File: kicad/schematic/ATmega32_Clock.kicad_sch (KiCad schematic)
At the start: 0 parts

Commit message: Restored full KiCad schematic and PCB layouts from original AI generation prior to truncation
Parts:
- added C1, C2: 22pF, Capacitor_THT:C_Disc_D3.0mm_W1.6mm_P2.50mm, symbol Device:C
- added C3, C4: 100nF, Capacitor_THT:C_Disc_D3.0mm_W1.6mm_P2.50mm, symbol Device:C
- added D1: STATUS, LED_THT:LED_D3.0mm, symbol Device:LED
- added D2: TASK, LED_THT:LED_D3.0mm, symbol Device:LED
- added J1: USART, Connector_PinHeader_2.54mm:PinHeader_1x02_P2.54mm_Vertical, symbol Connector_Generic:Conn_01x02
- added J2: ISP, Connector_PinHeader_2.54mm:PinHeader_2x03_P2.54mm_Vertical, symbol Connector_Generic:Conn_02x03_Odd_Even
- added R1, R2, R3, R4: 10K, Resistor_THT:R_Axial_DIN0207_L6.3mm_D2.5mm_P10.16mm_Horizontal, symbol Device:R
- added R5, R6: 330R, Resistor_THT:R_Axial_DIN0207_L6.3mm_D2.5mm_P10.16mm_Horizontal, symbol Device:R
- added SW1: RESET, Button_Switch_THT:SW_PUSH_6mm, symbol Switch:SW_Push
- added SW2: SET, Button_Switch_THT:SW_PUSH_6mm, symbol Switch:SW_Push
- added SW3: INCREMENT, Button_Switch_THT:SW_PUSH_6mm, symbol Switch:SW_Push
- added SW4: CLK_RST, Button_Switch_THT:SW_PUSH_6mm, symbol Switch:SW_Push
- added U1: ATmega32A-P, Package_DIP:DIP-40_W15.24mm, symbol MCU_Microchip_ATmega:ATmega32A-P
- added Y1: 8MHz, Crystal:Crystal_HC49-4H_Vertical, symbol Device:Crystal
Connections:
- new net: R1.2, SW1.2
- new net: R2.2, SW2.2
- new net: R3.2, SW3.2
- new net: R4.2, SW4.2
- new net: D1.1 (K), R5.2
- new net: D2.1 (K), R6.2
- new net GND: C1.2, C2.2, D1.2 (A), D2.2 (A), SW1.1, SW2.1, SW3.1, SW4.1
- new net VCC: R1.1, R2.1, R3.1, R4.1
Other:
- note added: "BUTTONS: SET(PA0) INC(PA1) RST(PA2) Active-low, 10K pull-ups"
- note added: "CLOCK: 8MHz Crystal 22pF load caps"
- note added: "LEDs: STATUS(PB0) TASK(PB1) 330R current limiters"
- note added: "TIMER1 CTC: OCR1A = 8000000/(1024*1) - 1 = 7812 Interrupt Rate: 1 Hz (1 second) Prescaler: 1024 | F_CPU: 8 MHz"

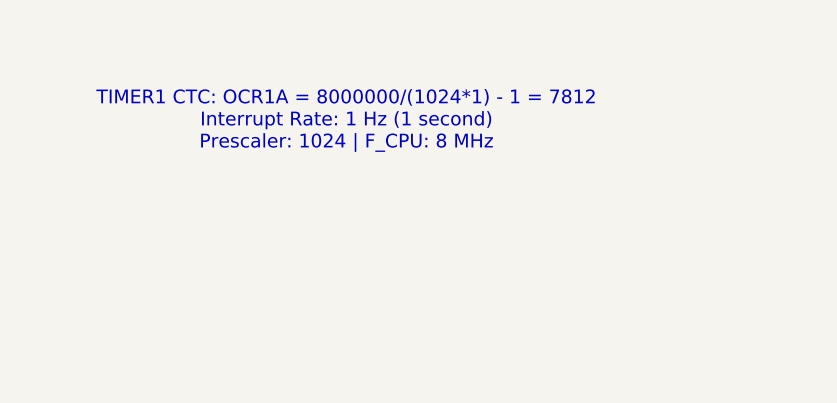
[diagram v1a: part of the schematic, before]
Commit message: Updated all documentation to reflect 10ms (100Hz) timer configuration
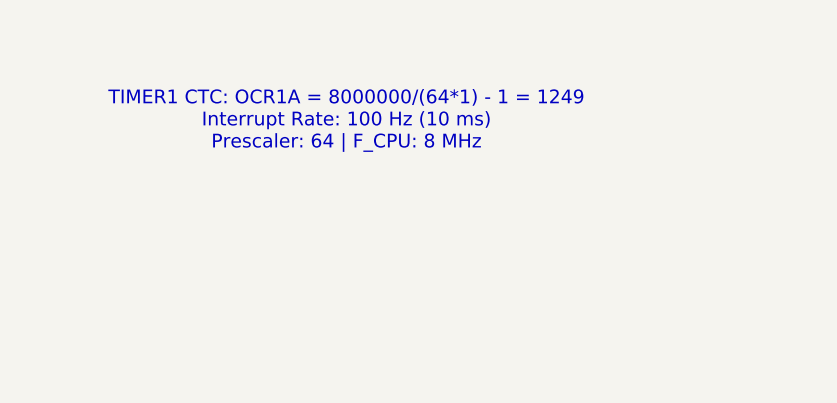
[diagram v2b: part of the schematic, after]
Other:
- note added: "TIMER1 CTC: OCR1A = 8000000/(64*1) - 1 = 1249 Interrupt Rate: 100 Hz (10 ms) Prescaler: 64 | F_CPU: 8 MHz"
- note removed: "TIMER1 CTC: OCR1A = 8000000/(1024*1) - 1 = 7812 Interrupt Rate: 1 Hz (1 second) Prescaler: 1024 | F_CPU: 8 MHz"
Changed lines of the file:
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@@
     (rev "1.0")
     (company "CT_321 PBL Project 08")
-    (comment 1 "Timer1 CTC | 8MHz Crystal | Prescaler 1024 | OCR1A=7812 | 1Hz Interrupt")
+    (comment 1 "Timer1 CTC | 8MHz Crystal | Prescaler 64 | OCR1A=1249 | 100Hz Interrupt")
     (comment 2 "Status LED: PB0 toggles 2s | Task LED: PB1 flashes 5s | USART 9600")
   )
@@
   (wire (pts (xy 121.92 73.66) (xy 121.92 76.2)) (stroke (width 0) (type default)))
   ;; ============= Text annotations =============
-  (text "TIMER1 CTC: OCR1A = 8000000/(1024*1) - 1 = 7812\nInterrupt Rate: 1 Hz (1 second)\nPrescaler: 1024 | F_CPU: 8 MHz"
+  (text "TIMER1 CTC: OCR1A = 8000000/(64*1) - 1 = 1249\nInterrupt Rate: 100 Hz (10 ms)\nPrescaler: 64 | F_CPU: 8 MHz"
     (at 30.48 44.45 0) (effects (font (size 1.524 1.524)))
   )

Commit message: Fixed KiCad schematic load error by clearing corrupt lib_symbols cache
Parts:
- removed C1, C2: 22pF, Capacitor_THT:C_Disc_D3.0mm_W1.6mm_P2.50mm, symbol Device:C
- removed C3, C4: 100nF, Capacitor_THT:C_Disc_D3.0mm_W1.6mm_P2.50mm, symbol Device:C
- removed D1: STATUS, LED_THT:LED_D3.0mm, symbol Device:LED
- removed D2: TASK, LED_THT:LED_D3.0mm, symbol Device:LED
- removed J1: USART, Connector_PinHeader_2.54mm:PinHeader_1x02_P2.54mm_Vertical, symbol Connector_Generic:Conn_01x02
- removed J2: ISP, Connector_PinHeader_2.54mm:PinHeader_2x03_P2.54mm_Vertical, symbol Connector_Generic:Conn_02x03_Odd_Even
- removed R1, R2, R3, R4: 10K, Resistor_THT:R_Axial_DIN0207_L6.3mm_D2.5mm_P10.16mm_Horizontal, symbol Device:R
- removed R5, R6: 330R, Resistor_THT:R_Axial_DIN0207_L6.3mm_D2.5mm_P10.16mm_Horizontal, symbol Device:R
- removed SW1: RESET, Button_Switch_THT:SW_PUSH_6mm, symbol Switch:SW_Push
- removed SW2: SET, Button_Switch_THT:SW_PUSH_6mm, symbol Switch:SW_Push
- removed SW3: INCREMENT, Button_Switch_THT:SW_PUSH_6mm, symbol Switch:SW_Push
- removed SW4: CLK_RST, Button_Switch_THT:SW_PUSH_6mm, symbol Switch:SW_Push
- removed U1: ATmega32A-P, Package_DIP:DIP-40_W15.24mm, symbol MCU_Microchip_ATmega:ATmega32A-P
- removed Y1: 8MHz, Crystal:Crystal_HC49-4H_Vertical, symbol Device:Crystal
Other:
- note removed: "BUTTONS: SET(PA0) INC(PA1) RST(PA2) Active-low, 10K pull-ups"
- note removed: "CLOCK: 8MHz Crystal 22pF load caps"
- note removed: "LEDs: STATUS(PB0) TASK(PB1) 330R current limiters"
- note removed: "TIMER1 CTC: OCR1A = 8000000/(64*1) - 1 = 1249 Interrupt Rate: 100 Hz (10 ms) Prescaler: 64 | F_CPU: 8 MHz"
